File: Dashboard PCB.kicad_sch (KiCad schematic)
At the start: 36 parts, among them J1 Controls_Leader_Export_02x06, J4 FAN_CTRL_01x02, J5 Horn_In_01x02, J6 Horn_Out_01x02

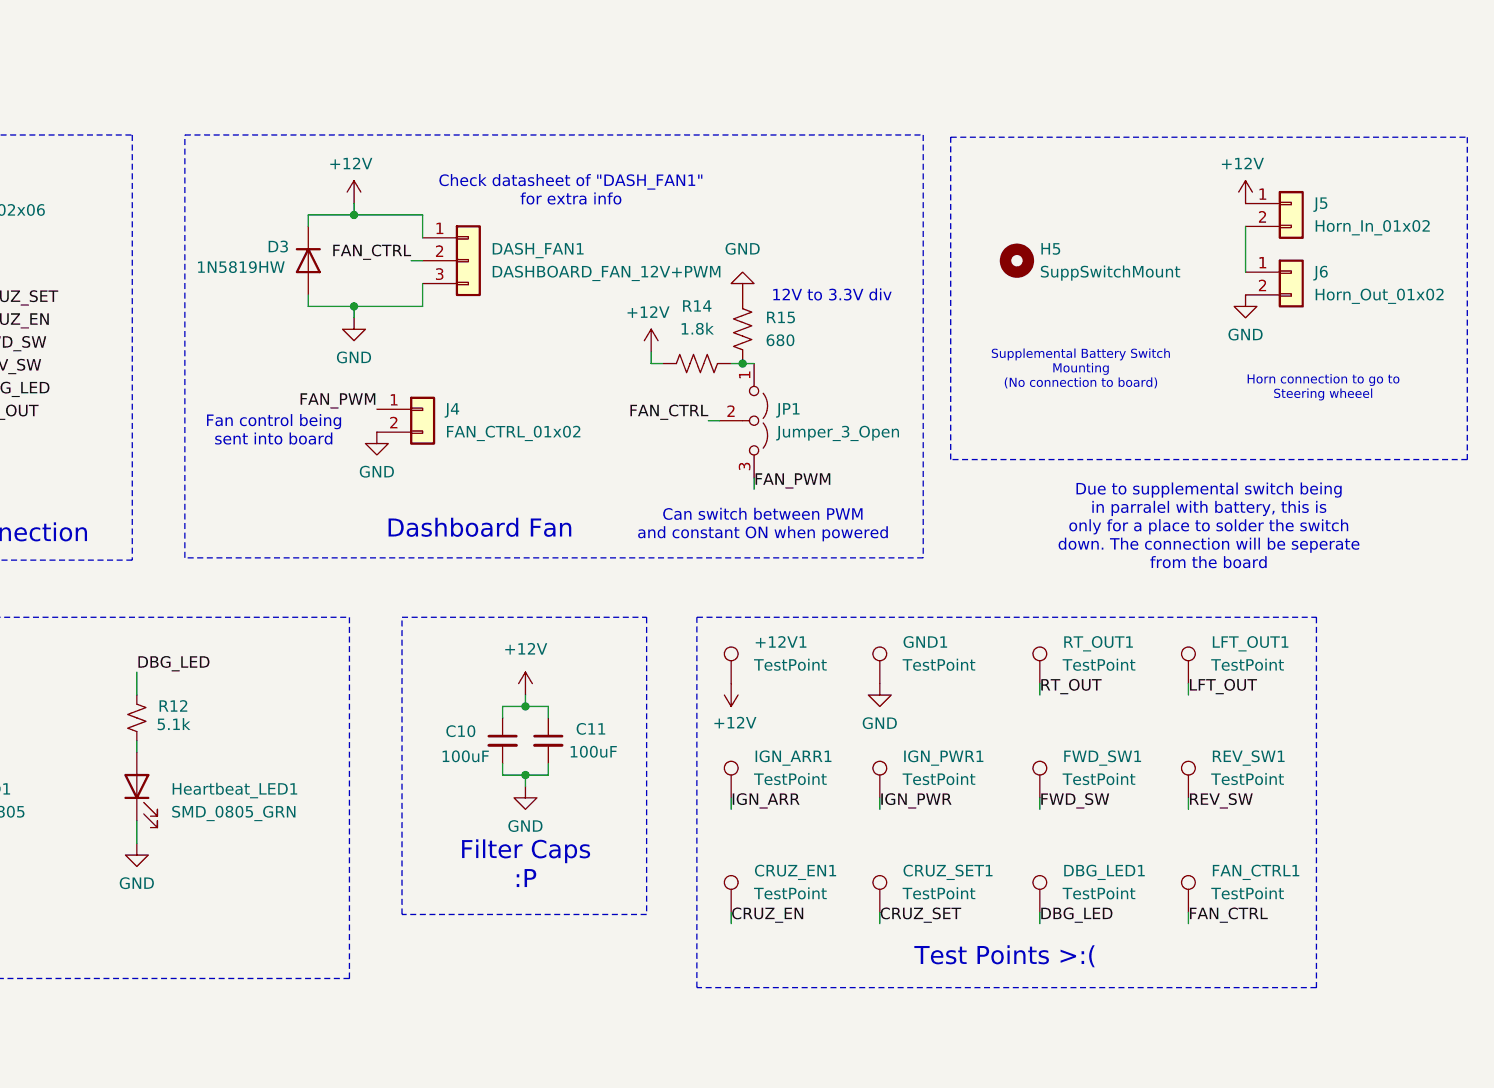
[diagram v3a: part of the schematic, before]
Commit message: Fixed fan and rot switch
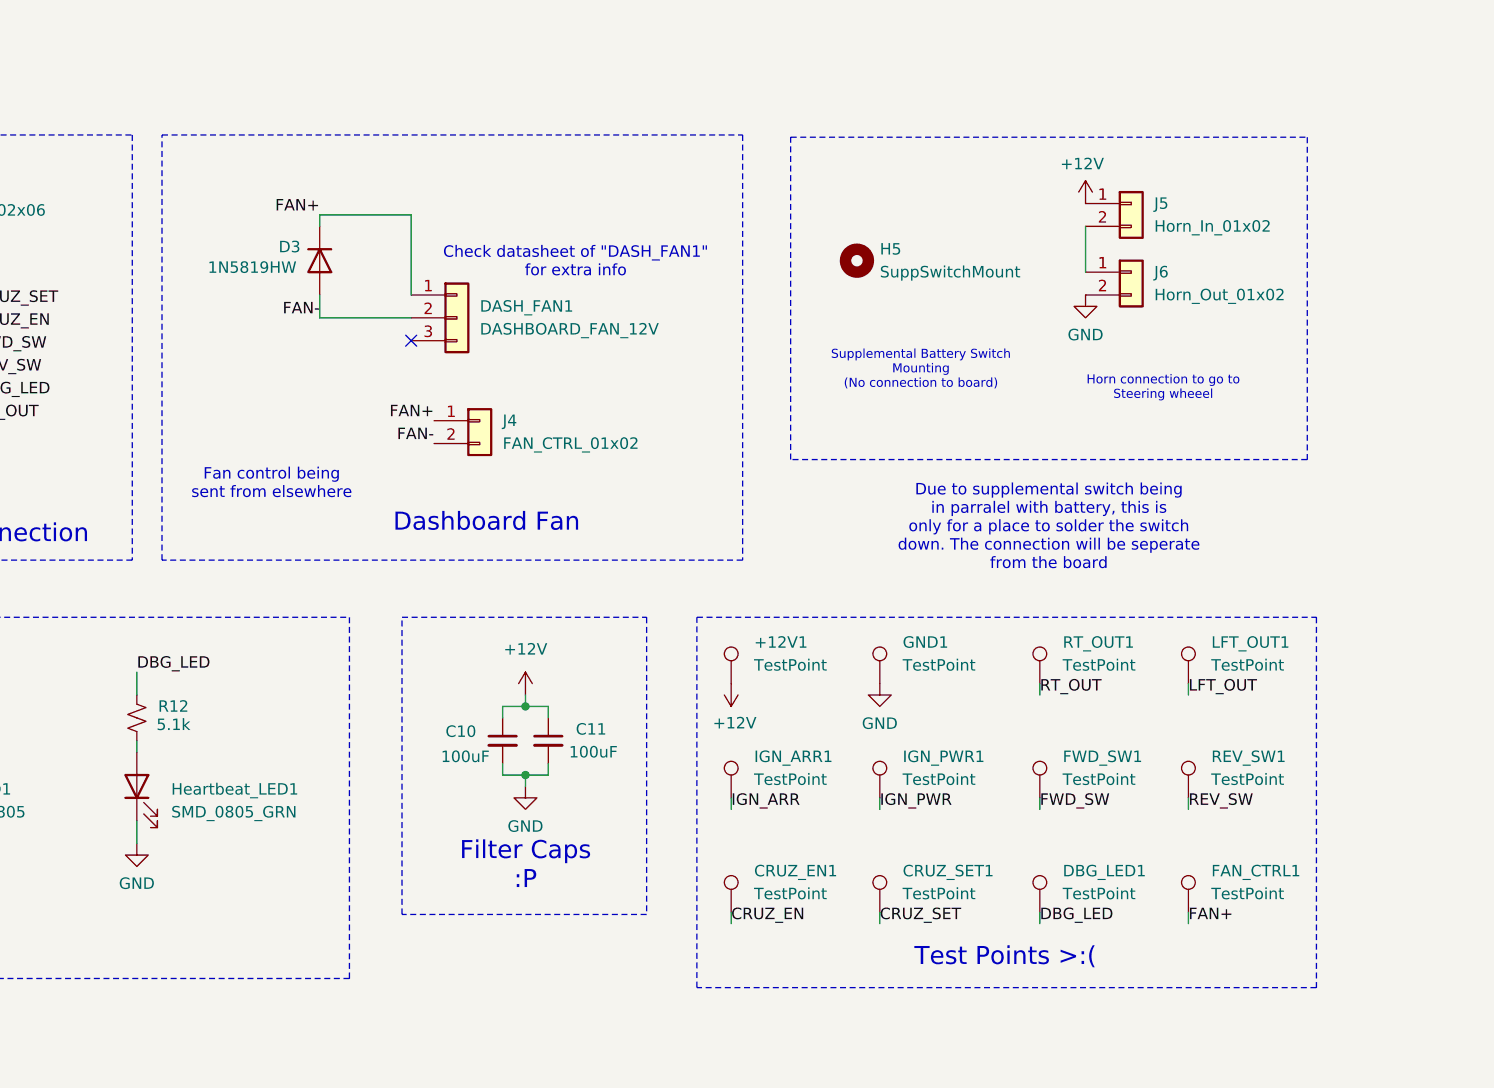
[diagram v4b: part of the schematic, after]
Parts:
- removed JP1: Jumper_3_Open, Jumper:SolderJumper-3_P1.3mm_Open_RoundedPad1.0x1.5mm, symbol Jumper:Jumper_3_Open
- removed R14: 1.8k, Resistor_SMD:R_0805_2012Metric, symbol Device:R_US
- removed R15: 680, Resistor_SMD:R_0805_2012Metric, symbol Device:R_US
- DASH_FAN1: value DASHBOARD_FAN_12V+PWM -> DASHBOARD_FAN_12V
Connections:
- net FAN_PWM is gone; now on net FAN+: J4.1 (Pin_1)
- net +12V: no longer D3.1 (K), DASH_FAN1.1 (Pin_1)
- net GND: no longer D3.2 (A), DASH_FAN1.3 (Pin_3), J4.2 (Pin_2)
- net FAN_CTRL renamed FAN+
- net FAN+: now also D3.1 (K), DASH_FAN1.1 (Pin_1); no longer DASH_FAN1.2 (Pin_2)
- new net FAN-: D3.2 (A), DASH_FAN1.2 (Pin_2), J4.2 (Pin_2)
- no-connect marks 0 -> 1
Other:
- note added: "Fan control being sent from elsewhere"
- note removed: "12V to 3.3V div"
- note removed: "Can switch between PWM and constant ON when powered"
- note removed: "Fan control being sent into board"
- moved on the sheet: D3, DASH_FAN1, H5, J4, J5, J6

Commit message: r pt 2
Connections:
- net +12V: now also R12.1, R13.1
- net BPS_HZD: now also BPS_HZD_OUT1.2 (Pin_2); no longer R13.1
- net DBG_LED: now also Heartbeat_LED1.1 (K); no longer R12.1
- net GND: no longer BPS_HZD_OUT1.2 (Pin_2), Heartbeat_LED1.1 (K)
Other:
- note added: "HZD and BPS and ctrled thru gnd"
- moved on the sheet: BPS_HZD_OUT1, Heartbeat_LED1, LFT_LED1, R10, R11, R12, R13, RT_LED1

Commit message: Changed layout, added 3d models
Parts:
- added J2, J7: Conn_02x03_CAN, Connector_Molex:Molex_Micro-Fit_3.0_43045-0600_2x03_P3.00mm_Horizontal, symbol Connector_Generic:Conn_02x03_Top_Bottom
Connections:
- new net CAN+12V: J2.3 (Pin_3), J7.3 (Pin_3)
- new net CAN-H: J2.6 (Pin_6), J7.6 (Pin_6)
- new net CAN-L: J2.5 (Pin_5), J7.5 (Pin_5)
- new net CANGND: J2.2 (Pin_2), J7.2 (Pin_2)
- no-connect marks 1 -> 5
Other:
- note added: "CAN-to-CAN out"

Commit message: Fixed stuff
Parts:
- added BPS_HZD1: TestPoint, TestPoint:TestPoint_Pad_1.0x1.0mm, symbol Connector:TestPoint
- +12V1, CRUZ_EN1, CRUZ_SET1, DBG_LED1, FAN_CTRL1, FWD_SW1, GND1, IGN_ARR1, IGN_PWR1, LFT_OUT1, REV_SW1, RT_OUT1: footprint Connector_PinHeader_2.54mm:PinHeader_1x01_P2.54mm_Vertical -> TestPoint:TestPoint_Pad_1.0x1.0mm
- Heartbeat_LED1, LFT_LED1, RT_LED1: P/N (none) -> APTD2012LCGCK
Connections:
- net BPS_HZD: now also BPS_HZD1.1
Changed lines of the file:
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@@
 	(text "HZD and BPS and ctrled\nthru gnd"
 		(exclude_from_sim no)
-		(at 60.706 143.764 0)
+		(at 62.484 140.462 0)
 		(effects
 			(font
@@
 			)
 		)
-		(property "Footprint" "Connector_PinHeader_2.54mm:PinHeader_1x01_P2.54mm_Vertical"
+		(property "Footprint" "TestPoint:TestPoint_Pad_1.0x1.0mm"
 			(at 213.36 121.92 0)
 			(effects
@@
 			)
 		)
-		(property "Datasheet" "~"
+		(property "Datasheet" "https://www.kingbrightusa.com/images/catalog/SPEC/APTD2012LCGCK.pdf"
 			(at 132.08 133.35 0)
 			(effects
@@
 			)
 		)
+		(property "P/N" "APTD2012LCGCK"
+			(at 132.08 133.35 90)
+			(effects
+				(font
+					(size 1.27 1.27)
+				)
+				(hide yes)
+			)
+		)
 		(pin "2"
 		)
@@
 			)
 		)
-		(property "Footprint" "Connector_PinHeader_2.54mm:PinHeader_1x01_P2.54mm_Vertical"
+		(property "Footprint" "TestPoint:TestPoint_Pad_1.0x1.0mm"
 			(at 247.65 134.62 0)
 			(effects
@@
 			)
 		)
-		(property "Footprint" "Connector_PinHeader_2.54mm:PinHeader_1x01_P2.54mm_Vertical"
+		(property "Footprint" "TestPoint:TestPoint_Pad_1.0x1.0mm"
 			(at 196.85 147.32 0)
 			(effects
@@
 			)
 		)
-		(property "Datasheet" "~"
+		(property "Datasheet" "https://www.kingbrightusa.com/images/catalog/SPEC/APTD2012LCGCK.pdf"
 			(at 102.87 133.35 0)
 			(effects
@@
 			)
 		)
+		(property "P/N" "APTD2012LCGCK"
+			(at 102.87 133.35 90)
+			(effects
+				(font
+					(size 1.27 1.27)
+				)
+				(hide yes)
+			)
+		)
 		(pin "2"
 		)
@@
 			)
 		)
-		(property "Footprint" "Connector_PinHeader_2.54mm:PinHeader_1x01_P2.54mm_Vertical"
+		(property "Footprint" "TestPoint:TestPoint_Pad_1.0x1.0mm"
 			(at 231.14 147.32 0)
 			(effects
@@
 			)
 		)
-		(property "Footprint" "Connector_PinHeader_2.54mm:PinHeader_1x01_P2.54mm_Vertical"
+		(property "Footprint" "TestPoint:TestPoint_Pad_1.0x1.0mm"
 			(at 213.36 147.32 0)
 			(effects
@@
 	(symbol
 		(lib_id "Connector:TestPoint")
+		(at 43.18 140.97 180)
+		(unit 1)
+		(exclude_from_sim no)
+		(in_bom yes)
+		(on_board yes)
+		(dnp no)
+		(fields_autoplaced yes)
+		(property "Reference" "BPS_HZD1"
+			(at 45.72 143.0019 0)
+			(effects
+				(font
+					(size 1.27 1.27)
+				)
+				(justify right)
+			)
+		)
+		(property "Value" "TestPoint"
+			(at 45.72 145.5419 0)
+			(effects
+				(font
+					(size 1.27 1.27)
+				)
+				(justify right)
+			)
+		)
+		(property "Footprint" "TestPoint:TestPoint_Pad_1.0x1.0mm"
+			(at 38.1 140.97 0)
+			(effects
+				(font
+					(size 1.27 1.27)
+				)
+				(hide yes)
+			)
+		)
+		(property "Datasheet" "~"
+			(at 38.1 140.97 0)
+			(effects
+				(font
+					(size 1.27 1.27)
+				)
+				(hide yes)
+			)
+		)
+		(property "Description" "test point"
+			(at 43.18 140.97 0)
+			(effects
+				(font
+					(size 1.27 1.27)
+				)
+				(hide yes)
+			)
+		)
+		(pin "1"
+		)
+		(instances
+			(project "Dashboard PCB"
+				(path "/db66d699-14af-49af-adc9-07d31d38aebd"
+					(reference "BPS_HZD1")
+					(unit 1)
+				)
+			)
+		)
+	)
+	(symbol
+		(lib_id "Connector:TestPoint")
 		(at 191.77 121.92 0)
 		(unit 1)
@@
 			)
 		)
-		(property "Footprint" "Connector_PinHeader_2.54mm:PinHeader_1x01_P2.54mm_Vertical"
+		(property "Footprint" "TestPoint:TestPoint_Pad_1.0x1.0mm"
 			(at 196.85 121.92 0)
 			(effects
@@
 			)
 		)
-		(property "Footprint" "Connector_PinHeader_2.54mm:PinHeader_1x01_P2.54mm_Vertical"
+		(property "Footprint" "TestPoint:TestPoint_Pad_1.0x1.0mm"
 			(at 196.85 134.62 0)
 			(effects
@@
 			)
 		)
-		(property "Footprint" "Connector_PinHeader_2.54mm:PinHeader_1x01_P2.54mm_Vertical"
+		(property "Footprint" "TestPoint:TestPoint_Pad_1.0x1.0mm"
 			(at 213.36 134.62 0)
 			(effects
@@
 			)
 		)
-		(property "Footprint" "Connector_PinHeader_2.54mm:PinHeader_1x01_P2.54mm_Vertical"
+		(property "Footprint" "TestPoint:TestPoint_Pad_1.0x1.0mm"
 			(at 247.65 121.92 0)
 			(effects
@@
 			)
 		)
-		(property "Footprint" "Connector_PinHeader_2.54mm:PinHeader_1x01_P2.54mm_Vertical"
+		(property "Footprint" "TestPoint:TestPoint_Pad_1.0x1.0mm"
 			(at 247.65 147.32 0)
 			(effects
@@
 			)
 		)
-		(property "Footprint" "Connector_PinHeader_2.54mm:PinHeader_1x01_P2.54mm_Vertical"
+		(property "Footprint" "TestPoint:TestPoint_Pad_1.0x1.0mm"
 			(at 231.14 121.92 0)
 			(effects
@@
 			)
 		)
-		(property "Footprint" "Connector_PinHeader_2.54mm:PinHeader_1x01_P2.54mm_Vertical"
+		(property "Footprint" "TestPoint:TestPoint_Pad_1.0x1.0mm"
 			(at 231.14 134.62 0)
 			(effects
@@
 			)
 		)
-		(property "Datasheet" "~"
+		(property "Datasheet" "https://www.kingbrightusa.com/images/catalog/SPEC/APTD2012LCGCK.pdf"
 			(at 74.93 133.35 0)
 			(effects
@@
 			(effects
 				(font
+					(size 1.27 1.27)
+				)
+				(hide yes)
+			)
+		)
+		(property "P/N" "APTD2012LCGCK"
+			(at 74.93 133.35 90)
+			(effects
+				(font

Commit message: More stuff
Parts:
- J7: footprint Connector_Molex:Molex_Micro-Fit_3.0_43045-0600_2x03_P3.00mm_Horizontal -> Connector_Molex:Molex_Micro-Fit_3.0_43045-0400_2x02_P3.00mm_Horizontal; symbol Connector_Generic:Conn_02x03_Top_Bottom -> Connector_Generic:Conn_02x02_Top_Bottom
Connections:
- net CAN+12V: now also J7.2 (Pin_2); no longer J7.3 (Pin_3)
- net CAN-H: now also J7.4 (Pin_4); no longer J7.6 (Pin_6)
- net CAN-L: now also J7.3 (Pin_3); no longer J7.5 (Pin_5)
- net CANGND: now also J7.1 (Pin_1); no longer J7.2 (Pin_2)
- no-connect marks 5 -> 3
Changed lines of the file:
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@@
-	)
-	(no_connect
-		(at 209.55 50.8)
 	)
 	(no_connect
@@
 	(no_connect
 		(at 238.76 50.8)
-	)
-	(no_connect
-		(at 209.55 38.1)
 	)
 	(wire
@@
 	)
 	(symbol
-		(lib_id "Connector_Generic:Conn_02x03_Top_Bottom")
+		(lib_id "Connector_Generic:Conn_02x02_Top_Bottom")
 		(at 212.09 45.72 90)
 		(unit 1)
@@
 			)
 		)
-		(property "Footprint" "Connector_Molex:Molex_Micro-Fit_3.0_43045-0600_2x03_P3.00mm_Horizontal"
+		(property "Footprint" "Connector_Molex:Molex_Micro-Fit_3.0_43045-0400_2x02_P3.00mm_Horizontal"
 			(at 212.09 45.72 0)
 			(effects
@@
 			)
 		)
-		(property "Description" "Generic connector, double row, 02x03, top/bottom pin numbering scheme (row 1: 1...pins_per_row, row2: pins_per_row+1 ... num_pins), script generated (kicad-library-utils/schlib/autogen/connector/)"
+		(property "Description" "Generic connector, double row, 02x02, top/bottom pin numbering scheme (row 1: 1...pins_per_row, row2: pins_per_row+1 ... num_pins), script generated (kicad-library-utils/schlib/autogen/connector/)"
 			(at 212.09 45.72 0)
 			(effects
@@
 		(pin "2"
 		)
-		(pin "6"
-		)
-		(pin "5"
-		)
 		(instances
